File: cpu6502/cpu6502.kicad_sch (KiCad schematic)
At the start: 21 parts, among them J1 Conn_01x02, J2 Conn_02x05_Odd_Even, U1 74LS161, U2 W65C02SxP / MC6802 / R6502, U3 74LS573, U4 74LS573, U5 74LS573, U6 74LS245, X1 8.0 MHz

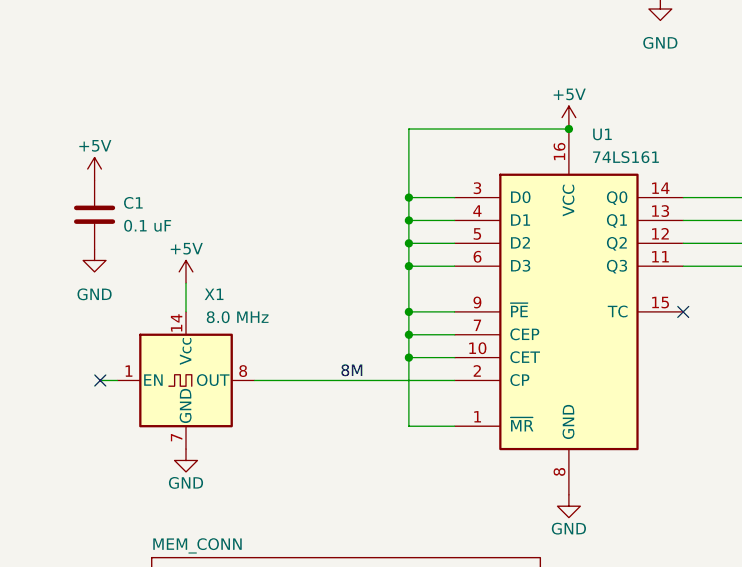
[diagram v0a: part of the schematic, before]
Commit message: Moved devices around and size reduced board.
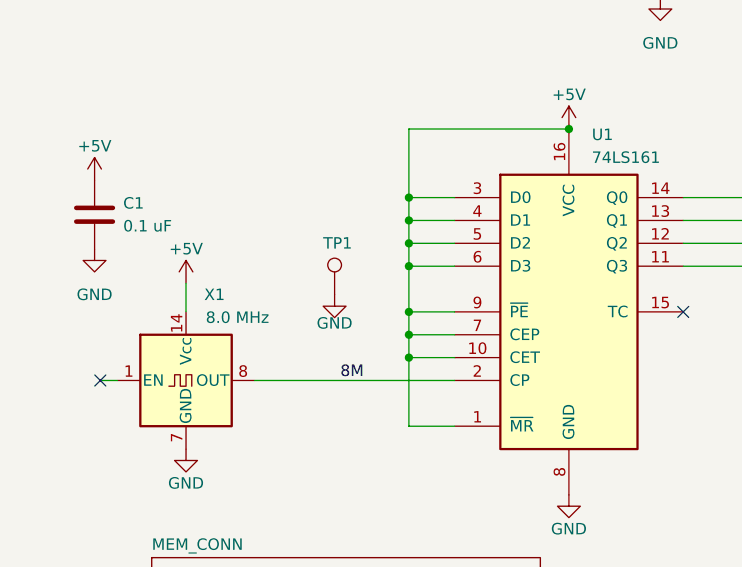
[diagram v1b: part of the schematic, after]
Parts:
- added TP1: TestPoint, TestPoint:TestPoint_Pad_2.0x2.0mm, symbol Connector:TestPoint
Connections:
- net GND: now also TP1.1
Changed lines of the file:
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@@
+    (pin "1")
+  )
+  (symbol (lib_id "power:GND") (at 45.085 138.43 0) (unit 1)
+    (in_bom yes) (on_board yes)
+    (property "Reference" "#PWR0101" (id 0) (at 45.085 144.78 0)
+      (effects (font (size 1.27 1.27)) hide)
+    )
+    (property "Value" "GND" (id 1) (at 45.085 141.605 0))
+    (property "Footprint" "" (id 2) (at 45.085 138.43 0)
+      (effects (font (size 1.27 1.27)) hide)
+    )
+    (property "Datasheet" "" (id 3) (at 45.085 138.43 0)
+      (effects (font (size 1.27 1.27)) hide)
+    )
     (pin "1")
   )
@@
     )
     (property "Datasheet" "" (id 3) (at 18.415 133.35 0)
+      (effects (font (size 1.27 1.27)) hide)
+    )
+    (pin "1")
+  )
+  (symbol (lib_id "Connector:TestPoint") (at 45.085 138.43 0) (unit 1)
+    (in_bom yes) (on_board yes)
+    (property "Reference" "TP1" (id 0) (at 43.815 132.715 0)
+      (effects (font (size 1.27 1.27)) (justify left))
+    )
+    (property "Value" "TestPoint" (id 1) (at 46.99 136.3979 0)
+      (effects (font (size 1.27 1.27)) (justify left) hide)
+    )
+    (property "Footprint" "TestPoint:TestPoint_Pad_2.0x2.0mm" (id 2) (at 50.165 138.43 0)
+      (effects (font (size 1.27 1.27)) hide)
+    )
+    (property "Datasheet" "~" (id 3) (at 50.165 138.43 0)
       (effects (font (size 1.27 1.27)) hide)
     )
@@
       (reference "#PWR036") (unit 1) (value "GND") (footprint "")
     )
-    (path "/7ed65a36-0033-45ba-8699-70a6490fe1a8/a1ea716f-d74a-42e1-a4ee-8077a999a4c6"
-      (reference "#PWR037") (unit 1) (value "+5V") (footprint "")
+    (path "/7ed65a36-0033-45ba-8699-70a6490fe1a8/572e22a4-5a36-492f-96f5-8653b2cdd6c0"
+      (reference "#PWR037") (unit 1) (value "GND") (footprint "")
     )
     (path "/7ed65a36-0033-45ba-8699-70a6490fe1a8/2192b315-909c-43ec-9a95-0e05dbfdb00f"
@@
       (reference "#PWR047") (unit 1) (value "GND") (footprint "")
     )
-    (path "/7ed65a36-0033-45ba-8699-70a6490fe1a8/10920450-f609-40a3-a196-107d35fca69b"
-      (reference "#PWR049") (unit 1) (value "+5V") (footprint "")
+    (path "/7ed65a36-0033-45ba-8699-70a6490fe1a8/b89a8f1d-13c2-4752-9d9c-a14a0015eb09"
+      (reference "#PWR048") (unit 1) (value "+5V") (footprint "")
     )
     (path "/7ed65a36-0033-45ba-8699-70a6490fe1a8/9dfd0efe-aaf7-4329-a280-909345173c10"
@@
       (reference "#PWR055") (unit 1) (value "GND") (footprint "")
     )
-    (path "/7ed65a36-0033-45ba-8699-70a6490fe1a8/2e1e0802-5dd8-4f18-beea-162baed3e4a2"
-      (reference "#PWR056") (unit 1) (value "GND") (footprint "")
-    )
     (path "/7ed65a36-0033-45ba-8699-70a6490fe1a8/89b44d99-a484-443a-84f7-d1e884a9b1f3"
       (reference "#PWR057") (unit 1) (value "GND") (footprint "")
@@
       (reference "#PWR066") (unit 1) (value "GND") (footprint "")
     )
+    (path "/7989795d-b5ea-462d-abd3-0ef6f2acf03b"
+      (reference "#PWR0101") (unit 1) (value "GND") (footprint "")
+    )
     (path "/f4ef7c09-905b-4928-877e-7b13f4d3d6aa"
       (reference "C1") (unit 1) (value "0.1 uF") (footprint "Capacitor_THT:C_Rect_L7.2mm_W3.0mm_P5.00mm_FKS2_FKP2_MKS2_MKP2")
@@
       (reference "J3") (unit 1) (value "Conn_02x21_Odd_Even") (footprint "Connector_PinHeader_2.54mm:PinHeader_2x21_P2.54mm_Vertical")
     )
+    (path "/7ed65a36-0033-45ba-8699-70a6490fe1a8/0f4a1487-ff45-48ec-b885-e5c18ebf0159"
+      (reference "J4") (unit 1) (value "Conn_01x02") (footprint "Connector_PinHeader_2.54mm:PinHeader_1x02_P2.54mm_Vertical")
+    )
+    (path "/7ed65a36-0033-45ba-8699-70a6490fe1a8/d19781b2-c162-4ff4-ab07-cdeb1e21cbb7"
+      (reference "J5") (unit 1) (value "Conn_01x02") (footprint "Connector_PinHeader_2.54mm:PinHeader_1x02_P2.54mm_Vertical")
+    )
     (path "/7ed65a36-0033-45ba-8699-70a6490fe1a8/e5be52e5-23ca-4ab0-b421-43ad1046b3bc"
       (reference "PS1") (unit 1) (value "TBA_2-1211") (footprint "CONV_TBA_2-1211")
@@
       (reference "R6") (unit 1) (value "1K") (footprint "Resistor_THT:R_Axial_DIN0207_L6.3mm_D2.5mm_P10.16mm_Horizontal")
     )
-    (path "/7ed65a36-0033-45ba-8699-70a6490fe1a8/1e3c63fb-9929-4c14-9a3c-27a01671aa2f"
+    (path "/7ed65a36-0033-45ba-8699-70a6490fe1a8/d9de125e-a9bd-4745-9145-00f9916e9989"
+      (reference "R7") (unit 1) (value "10.5K") (footprint "Resistor_THT:R_Axial_DIN0207_L6.3mm_D2.5mm_P10.16mm_Horizontal")
+    )
+    (path "/8f9f6e00-addf-4ad0-852d-50a5ef5cc377"
       (reference "TP1") (unit 1) (value "TestPoint") (footprint "TestPoint:TestPoint_Pad_2.0x2.0mm")
     )
-    (path "/7ed65a36-0033-45ba-8699-70a6490fe1a8/6d2ee18d-4651-4771-8b02-9b099e1ba550"
-      (reference "TP2") (unit 1) (value "TestPoint") (footprint "TestPoint:TestPoint_Pad_2.0x2.0mm")
-    )
-    (path "/7ed65a36-0033-45ba-8699-70a6490fe1a8/172917ed-5d4b-4d55-a475-9afd37ee96a8"
-      (reference "TP3") (unit 1) (value "TestPoint") (footprint "TestPoint:TestPoint_Pad_2.0x2.0mm")
-    )
     (path "/16a9718d-07c5-4df3-afa2-28f0913d98b2"
